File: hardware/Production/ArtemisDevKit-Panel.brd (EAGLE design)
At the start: 116.6 x 181.4 mm, 925 parts, among them J1 USB, J10 SMD, J11 SMD, J12 PTH, J13 USB, J14 PTH, J15 CORTEX_JTAG_DEBUG_MINIMUM_PTH, J16 CORTEX_JTAG_DEBUG_PTH, J17 QWIIC_RIGHT_ANGLE, J18 CAMERA-HIMAXBOTTOM-CONTACT, J19 SMD, J2 CORTEX_JTAG_DEBUG_MINIMUM_PTH, J20 PTH, J21 PTH, J22 PTH, J23 PTH, J24 PTH, J25 PTH, J26 PTH, J27 PTH, J28 PTH, J29 PTH, J3 CORTEX_JTAG_DEBUG_PTH, J30 PTH, J31 PTH, J32 PTH, J33 1X04_SMD_STRAIGHT_COMBO, J34 1X04_SMD_STRAIGHT_COMBO, J35 SMD, J36 SMD, J37 USB, J38 CORTEX_JTAG_DEBUG_MINIMUM_PTH, J39 CORTEX_JTAG_DEBUG_PTH, J4 SMD, J40 QWIIC_RIGHT_ANGLE, J41 CAMERA-HIMAXBOTTOM-CONTACT, J42 SMD, J43 PTH, J44 PTH, J45 PTH, J46 PTH, J47 PTH, J48 PTH, J49 PTH, J5 1X04_SMD_STRAIGHT_COMBO, J50 PTH, J51 1X04_SMD_STRAIGHT_COMBO, J52 1X04_SMD_STRAIGHT_COMBO, J53 SMD, J54 SMD, J55 USB, J56 CORTEX_JTAG_DEBUG_MINIMUM_PTH, J57 CORTEX_JTAG_DEBUG_PTH, J58 QWIIC_RIGHT_ANGLE, J59 CAMERA-HIMAXBOTTOM-CONTACT, J6 QWIIC_RIGHT_ANGLE, J60 SMD, J61 PTH, J62 PTH, J63 PTH, J64 PTH, J65 PTH, J66 PTH, J67 PTH, J68 PTH, J69 1X04_SMD_STRAIGHT_COMBO, J7 CAMERA-HIMAXBOTTOM-CONTACT, J70 1X04_SMD_STRAIGHT_COMBO, J71 SMD, J72 SMD, J8 PTH, J9 1X04_SMD_STRAIGHT_COMBO, U1 DAPLINK_KL26Z128VFM4, U10 DAPLINK_KL26Z128VFM4, U11 ARTEMIS_MODULESMD, U12 LIS2DH12, U13 AP2127K-1.8V, U14 3.3V, U15 DAPLINK_KL26Z128VFM4, U16 ARTEMIS_MODULESMD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

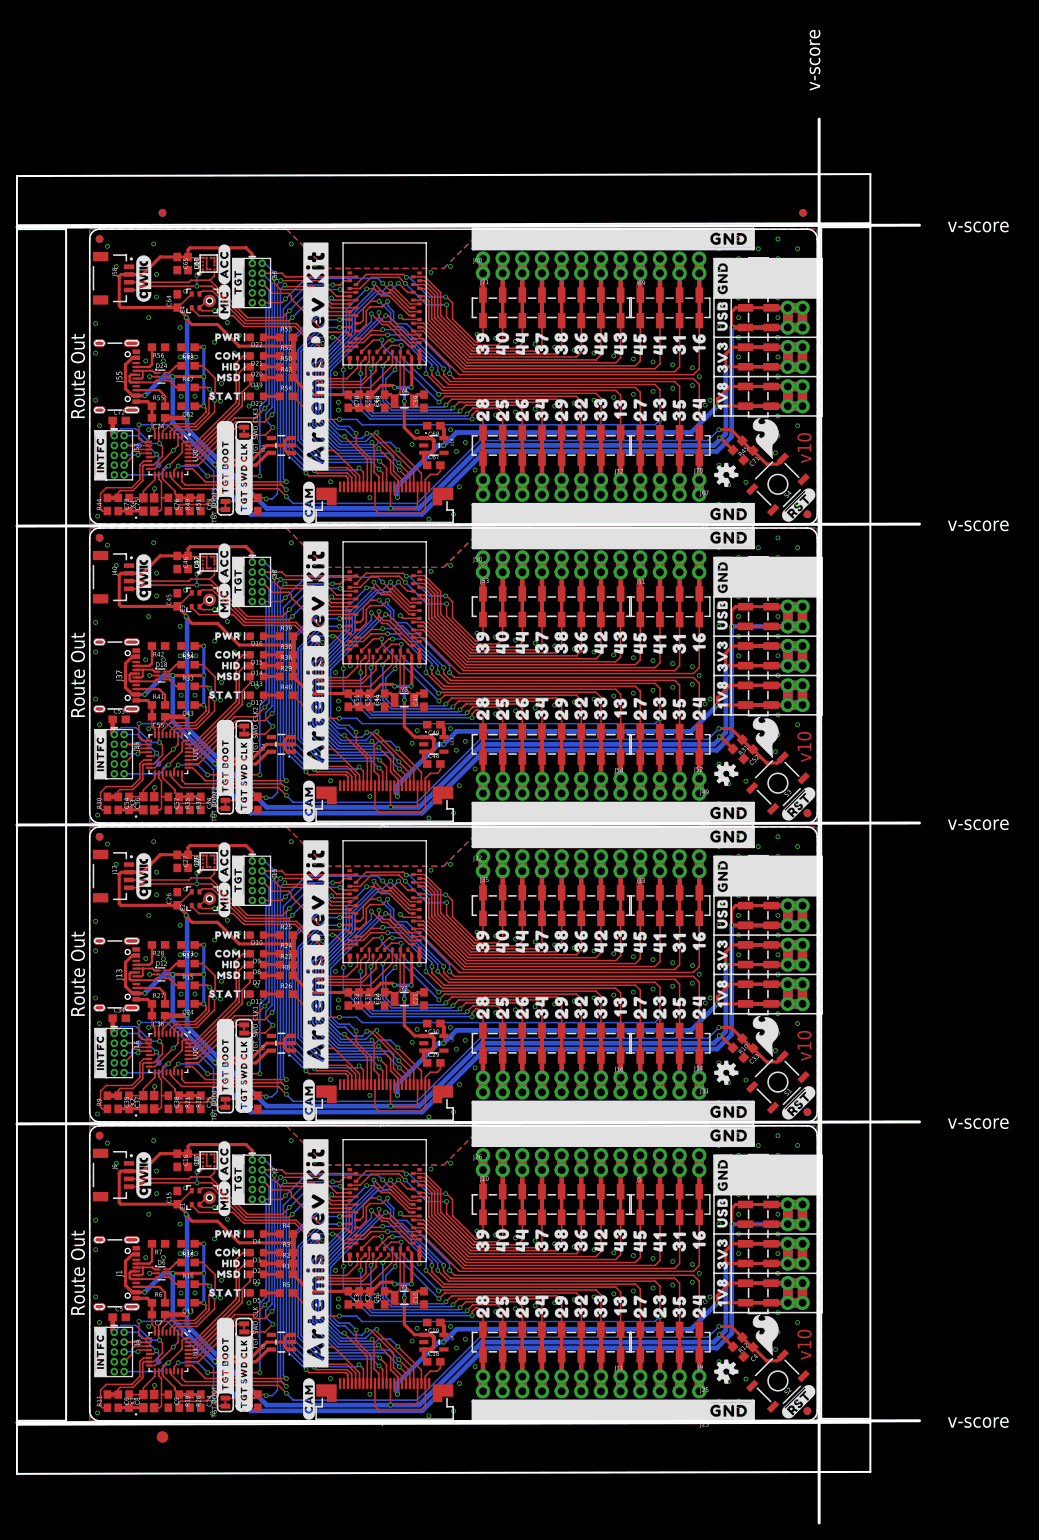
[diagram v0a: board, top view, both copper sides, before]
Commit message: fix crooked frame on panel
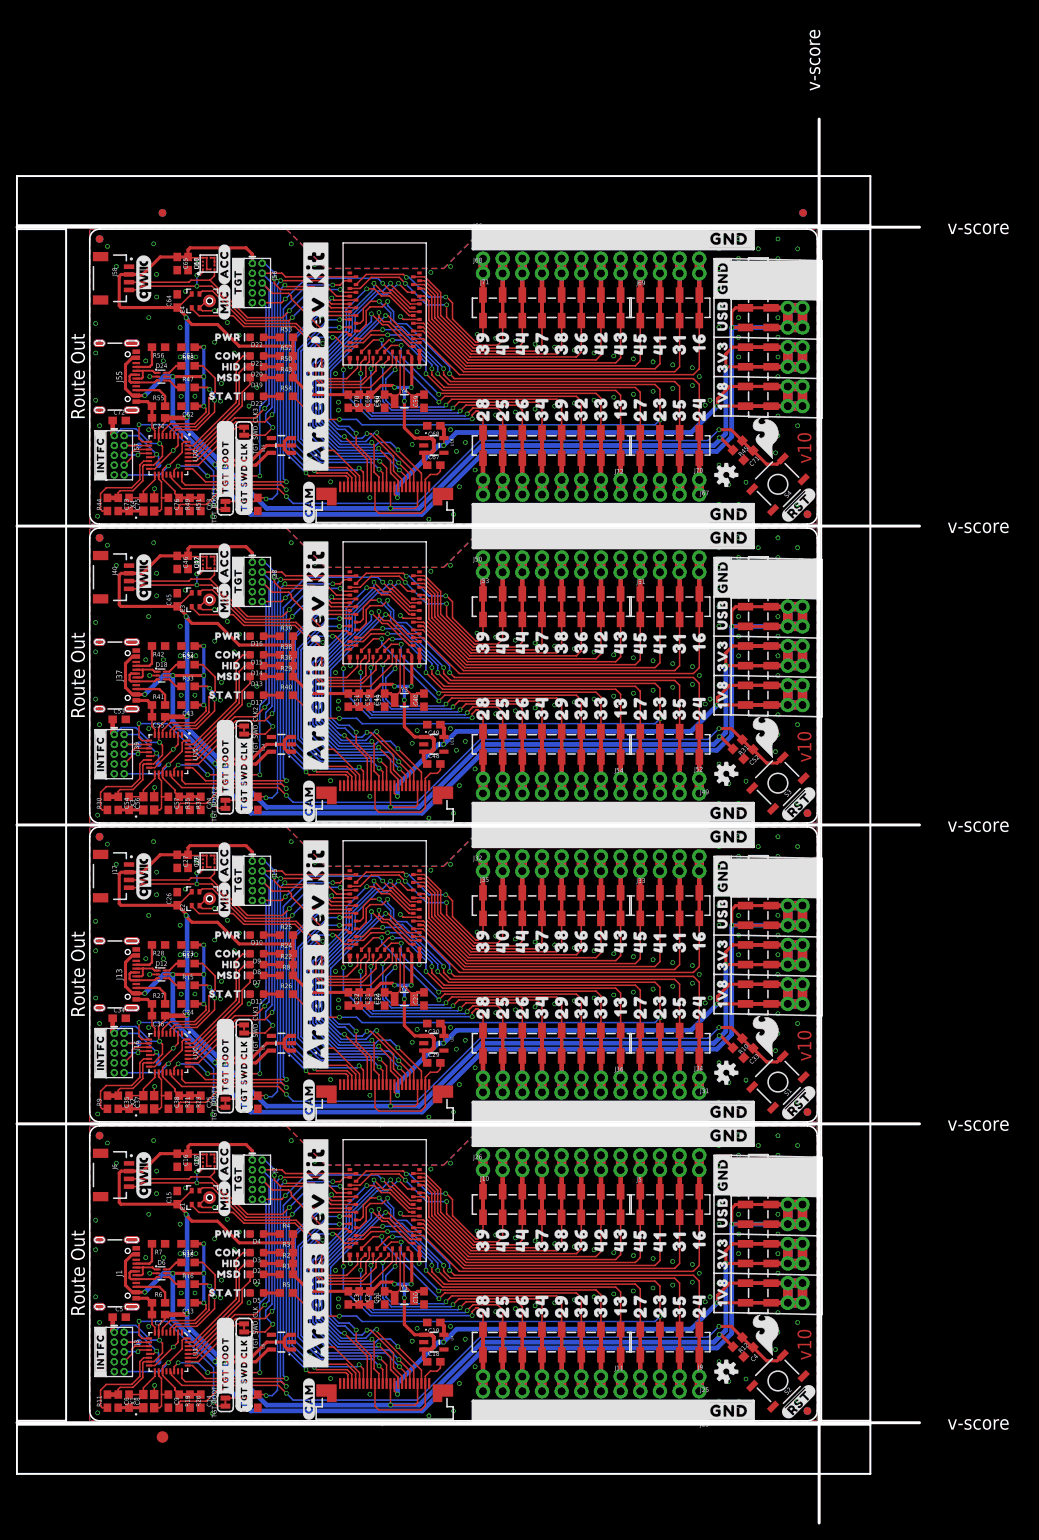
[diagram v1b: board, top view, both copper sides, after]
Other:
- outline, holes or cut-outs redrawn
